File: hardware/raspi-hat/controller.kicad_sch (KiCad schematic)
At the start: 5 parts, among them J1 Conn_02x05_Counter_Clockwise, U1 STSPIN32G4, Y1 Crystal_GND23_Small

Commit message: added op amp parts to pcb
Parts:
- added C8: 100n, Capacitor_SMD:C_0603_1608Metric, symbol Device:C
- added R20, R4: 0, Resistor_SMD:R_0603_1608Metric, symbol Device:R
- added R21: 68k, Resistor_SMD:R_0603_1608Metric, symbol Device:R
- added R22: 3k3, Resistor_SMD:R_0603_1608Metric, symbol Device:R
- U1: footprint QFN_IN32G4_STM -> Package_DFN_QFN:QFN-64-1EP_8x8mm_P0.4mm_EP6.5x6.5mm
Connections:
- net +3V3: now also U1.2 (VBAT), R20.1, R20.2, R4.1
- net GND: now also C8.2, R22.2
- net i2c_scl: now also U1.59 (PB8); no longer U1.48 (PA12)
- net pwr_on: now also U1.53 (PD2); no longer U1.5 (PC15)
- net at U1.13 (PA0): now also C8.1, R21.2, R22.1
- net shunt-amp/OP+: now reaches U1.14 (PA1)
- net shunt-amp/OPOUT: now reaches U1.15 (PA2)
- net shunt-amp/OP-: now reaches U1.16 (PA3)
- net shunt-amp1/OPOUT: now reaches U1.19 (PA6)
- net shunt-amp1/OP+: now reaches U1.20 (PA7)
- net shunt-amp1/OP-: now reaches U1.22 (PC5)
- net shunt-amp2/OP+: now reaches U1.23 (PB0)
- net shunt-amp2/OPOUT: now reaches U1.24 (PB1)
- net shunt-amp2/OP-: now reaches U1.25 (PB2)
- net inverter/LS1: now reaches U1.29 (GLS1)
- net inverter/LS2: now reaches U1.30 (GLS2)
- net inverter/LS3: now reaches U1.31 (GLS3)
- net inverter/OUT3: now reaches U1.36 (OUT3)
- net inverter/HS3: now reaches U1.37 (GHS3)
- net inverter/OUT2: now reaches U1.39 (OUT2)
- net inverter/HS2: now reaches U1.40 (GHS2)
- net inverter/OUT1: now reaches U1.42 (OUT1)
- net inverter/HS1: now reaches U1.43 (GHS1)
- net +12V: now reaches U1.61 (VM)
- net +12V: now also U1.64 (REGIN), R21.1
- net stspin_3V/SW: now reaches U1.62 (SW)
- net boot_1 renamed inverter/BOOT1
- net boot_2 renamed inverter/BOOT2
- net boot_3 renamed inverter/BOOT3
- new net stspin_3V/+3V3: R4.2
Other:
- added sheet inverter (inverter.kicad_sch)
- added sheet shunt-amp (shunt-amp.kicad_sch)
- added sheet shunt-amp1 (shunt-amp.kicad_sch)
- added sheet shunt-amp2 (shunt-amp.kicad_sch)
- added sheet stspin_3V (stspin_3V.kicad_sch)
- moved on the sheet: C1, C2, J1, Y1

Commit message: updatd ioc
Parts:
- added RV1: 10k, Potentiometer_SMD:Potentiometer_Bourns_3224W_Vertical, symbol Device:R_Potentiometer_Trim
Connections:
- net +3V3: now also RV1.1
- net GND: now also J1.9 (Pin_9), RV1.3
- net reset: now also J1.10 (Pin_10)
- net uart_tx: now reaches U1.45 (PA9)
- net uart_rx: now reaches U1.46 (PA10)
- net swd_io: now reaches U1.49 (PA13)
- net swd_io: now also J1.5 (Pin_5)
- net swd_clk: now reaches U1.50 (PA14)
- net swd_clk: now also J1.7 (Pin_7)
- net at U1.52 (SCREF): now also RV1.2
- net v_mc: now reaches J1.2 (Pin_2)
- net v_mc: now also J1.4 (Pin_4)
- net i2c_scl renamed boot
- net i2c_sda: no longer names the net of U1.60 (PB9)
- net inverter/OUT1 renamed phase_u
- net inverter/OUT2 renamed phase_v
- net inverter/OUT3 renamed phase_w
- net pwr_on: no longer names the net of U1.53 (PD2)

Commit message: added more parts
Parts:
- removed R20, R4: 0, Resistor_SMD:R_0603_1608Metric, symbol Device:R
- added J5: USB3_A, Connector_USB:USB3_A_Molex_48393-001, symbol Connector:USB3_A
- added JP2, JP3: Jumper_2_Open, Jumper:SolderJumper-2_P1.3mm_Open_TrianglePad1.0x1.5mm, symbol Jumper:Jumper_2_Open
- Y1: footprint Crystal:Crystal_SMD_0603-4Pin_6.0x3.5mm -> Crystal:Crystal_SMD_1210-4Pin_1.2x1.0mm_RotB
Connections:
- net +3V3: now also JP3.2 (B); no longer RV1.1, U1.1 (REG3V3), U1.2 (VBAT), U1.26 (VREF+), U1.27 (VDDA)
- net GND: now also J5.10 (SHIELD), J5.3 (D+), J5.4 (GND), J5.6 (SSRX+), J5.7 (DRAIN), J5.9 (SSTX+)
- net stspin_3V/+3V3: now also JP2.1 (A)
- net hall_1: now reaches U1.3 (PC13)
- net hall_1: now also J5.2 (D-)
- net hall_2: now reaches U1.4 (PC14)
- net hall_2: now also J5.5 (SSRX-)
- net hall_3: now reaches U1.5 (PC15)
- net hall_3: now also J5.8 (SSTX-)
- net power_on: now reaches U1.53 (PD2)
- new net +5V: J5.1 (VBUS)
- new net shunt-amp/+3V3: JP2.2 (B), JP3.1 (A), RV1.1, U1.1 (REG3V3), U1.2 (VBAT), U1.26 (VREF+), U1.27 (VDDA)
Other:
- moved on the sheet: C8, R21, R22

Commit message: added some layers
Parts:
- Y1: footprint Crystal:Crystal_SMD_1210-4Pin_1.2x1.0mm_RotB -> Crystal:Crystal_SMD_3225-4Pin_3.2x2.5mm
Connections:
- net at U1.6 (PF0): now also Y1.3; no longer Y1.4
- net at C1.1: now also Y1.4; no longer Y1.3
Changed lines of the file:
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@@
 			)
 		)
-		(property "Footprint" "Crystal:Crystal_SMD_1210-4Pin_1.2x1.0mm_RotB"
+		(property "Footprint" "Crystal:Crystal_SMD_3225-4Pin_3.2x2.5mm"
 			(at 185.42 189.23 0)
 			(effects

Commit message: routing
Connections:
- net shunt-amp/+3V3 is gone; now on net v_mc: JP2.2 (B), JP3.1 (A), RV1.1, U1.1 (REG3V3), U1.2 (VBAT), U1.26 (VREF+), U1.27 (VDDA)
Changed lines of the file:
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@@
+	)
+	(label "v_mc"
+		(at 396.24 26.67 0)
+		(effects
+			(font
+				(size 1.27 1.27)
+			)
+			(justify left bottom)
+		)
 	)
 	(label "v_mc"

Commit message: - some readability improvements - some routing updates
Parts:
- RV1: value 10k -> 50k
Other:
- moved on the sheet: JP3, RV1
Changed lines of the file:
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@@
 	)
 	(junction
+		(at 50.8 24.13)
+		(diameter 0)
+		(color 0 0 0 0)
+	)
+	(junction
 		(at 223.52 199.39)
 		(diameter 0)
@@
 	)
 	(junction
-		(at 35.56 24.13)
-		(diameter 0)
-		(color 0 0 0 0)
-	)
-	(junction
 		(at 254 26.67)
 		(diameter 0)
@@
 	(wire
 		(pts
-			(xy 336.55 134.62) (xy 349.25 134.62)
+			(xy 389.89 134.62) (xy 377.19 134.62)
 		)
 		(stroke
@@
 	(wire
 		(pts
-			(xy 49.53 26.67) (xy 95.25 26.67)
+			(xy 81.28 26.67) (xy 95.25 26.67)
+		)
+		(stroke
+			(width 0)
+			(type default)
+		)
+	)
+	(wire
+		(pts
+			(xy 50.8 24.13) (xy 396.24 24.13)
 		)
 		(stroke
@@
 	(wire
 		(pts
-			(xy 30.48 24.13) (xy 35.56 24.13)
+			(xy 30.48 24.13) (xy 50.8 24.13)
 		)
 		(stroke
@@
 	(wire
 		(pts
-			(xy 46.99 207.01) (xy 46.99 190.5)
-		)
-		(stroke
-			(width 0)
-			(type default)
-		)
-	)
-	(wire
-		(pts
 			(xy 77.47 76.2) (xy 86.36 76.2)
 		)
@@
 	(wire
 		(pts
-			(xy 336.55 143.51) (xy 349.25 143.51)
+			(xy 389.89 143.51) (xy 377.19 143.51)
 		)
 		(stroke
@@
 	(wire
 		(pts
-			(xy 250.19 176.53) (xy 248.92 176.53)
+			(xy 250.19 173.99) (xy 248.92 173.99)
 		)
 		(stroke
@@
 	(wire
 		(pts
-			(xy 254 180.34) (xy 254 241.3)
+			(xy 254 177.8) (xy 254 241.3)
 		)
 		(stroke
@@
 	(wire
 		(pts
-			(xy 254 172.72) (xy 254 26.67)
+			(xy 254 170.18) (xy 254 26.67)
 		)
 		(stroke
@@
 	(wire
 		(pts
-			(xy 336.55 135.89) (xy 349.25 135.89)
+			(xy 389.89 135.89) (xy 377.19 135.89)
 		)
 		(stroke
@@
 	(wire
 		(pts
-			(xy 35.56 24.13) (xy 396.24 24.13)
-		)
-		(stroke
-			(width 0)
-			(type default)
-		)
-	)
-	(wire
-		(pts
 			(xy 231.14 21.59) (xy 231.14 58.42)
 		)
@@
 	(wire
 		(pts
-			(xy 248.92 176.53) (xy 248.92 181.61)
+			(xy 248.92 173.99) (xy 248.92 181.61)
 		)
 		(stroke
@@
 	(wire
 		(pts
+			(xy 50.8 207.01) (xy 46.99 207.01)
+		)
+		(stroke
+			(width 0)
+			(type default)
+		)
+	)
+	(wire
+		(pts
 			(xy 363.22 147.32) (xy 363.22 241.3)
 		)
@@
 	(wire
 		(pts
-			(xy 336.55 142.24) (xy 349.25 142.24)
+			(xy 389.89 142.24) (xy 377.19 142.24)
 		)
 		(stroke
@@
 	(wire
 		(pts
-			(xy 336.55 138.43) (xy 349.25 138.43)
+			(xy 389.89 138.43) (xy 377.19 138.43)
 		)
 		(stroke
@@
 	(wire
 		(pts
-			(xy 46.99 190.5) (xy 35.56 190.5)
-		)
-		(stroke
-			(width 0)
-			(type default)
-		)
-	)
-	(wire
-		(pts
 			(xy 31.75 234.95) (xy 31.75 241.3)
 		)
@@
 	(wire
 		(pts
-			(xy 336.55 139.7) (xy 349.25 139.7)
+			(xy 389.89 139.7) (xy 377.19 139.7)
 		)
 		(stroke
@@
 	(wire
 		(pts
-			(xy 35.56 190.5) (xy 35.56 24.13)
+			(xy 50.8 24.13) (xy 50.8 207.01)
 		)
 		(stroke
@@
 	(wire
 		(pts
-			(xy 30.48 26.67) (xy 39.37 26.67)
+			(xy 30.48 26.67) (xy 71.12 26.67)
 		)
 		(stroke
@@
 	)
 	(label "shunt3_h"
-		(at 336.55 142.24 180)
+		(at 389.89 142.24 0)
 		(effects
 			(font
 				(size 1.27 1.27)
 			)
-			(justify right bottom)
+			(justify left bottom)
 		)
 	)
@@
 	)
 	(label "shunt2_l"
-		(at 336.55 139.7 180)
+		(at 389.89 139.7 0)
 		(effects
 			(font
 				(size 1.27 1.27)
 			)
-			(justify right bottom)
+			(justify left bottom)
 		)
 	)
@@
 	)
 	(label "shunt1_l"
-		(at 336.55 135.89 180)
+		(at 389.89 135.89 0)
 		(effects
 			(font
 				(size 1.27 1.27)
 			)
-			(justify right bottom)
+			(justify left bottom)
 		)
 	)
@@
 	)
 	(label "shunt3_l"
-		(at 336.55 143.51 180)
+		(at 389.89 143.51 0)
 		(effects
 			(font
 				(size 1.27 1.27)
 			)
-			(justify right bottom)
+			(justify left bottom)
 		)
 	)
 	(label "shunt2_h"
-		(at 336.55 138.43 180)
+		(at 389.89 138.43 0)
 		(effects
 			(font
 				(size 1.27 1.27)
 			)
-			(justify right bottom)
+			(justify left bottom)
 		)
 	)
@@
 	)
 	(label "shunt1_h"
-		(at 336.55 134.62 180)
+		(at 389.89 134.62 0)
 		(effects
 			(font
 				(size 1.27 1.27)
 			)
-			(justify right bottom)
+			(justify left bottom)
 		)
 	)
@@
 	(symbol
 		(lib_id "Jumper:Jumper_2_Open")
-		(at 44.45 26.67 180)
+		(at 76.2 26.67 180)
 		(unit 1)
 		(exclude_from_sim no)
@@
 		(dnp no)
 		(property "Reference" "JP3"
-			(at 38.1 28.194 0)
+			(at 69.85 28.194 0)
 			(effects
 				(font
@@
 		)
 		(property "Value" "Jumper_2_Open"
-			(at 37.846 30.48 0)
+			(at 69.596 30.48 0)
 			(effects
 				(font
@@
 		)
 		(property "Footprint" "Jumper:SolderJumper-2_P1.3mm_Open_TrianglePad1.0x1.5mm"
-			(at 44.45 26.67 0)
+			(at 76.2 26.67 0)
 			(effects
 				(font
@@
 		)
 		(property "Datasheet" "~"
-			(at 44.45 26.67 0)
+			(at 76.2 26.67 0)
 			(effects
 				(font
@@
 		)
 		(property "Description" "Jumper, 2-pole, open"
-			(at 44.45 26.67 0)
+			(at 76.2 26.67 0)
 			(effects
 				(font
@@
 	(symbol
 		(lib_id "Device:R_Potentiometer_Trim")
-		(at 254 176.53 0)
+		(at 254 173.99 0)
 		(mirror y)
 		(unit 1)
@@
 		(dnp no)
 		(property "Reference" "RV1"
-			(at 256.54 175.2599 0)
+			(at 256.54 172.7199 0)
 			(effects
 				(font
@@
 			)
 		)
-		(property "Value" "10k"
-			(at 254 174.498 90)
+		(property "Value" "50k"
+			(at 254 171.958 90)
 			(effects
 				(font
@@
 		)
 		(property "Footprint" "Potentiometer_SMD:Potentiometer_Bourns_3224W_Vertical"
-			(at 254 176.53 0)
+			(at 254 173.99 0)
 			(effects
 				(font
@@
 		)
 		(property "Datasheet" "~"
-			(at 254 176.53 0)
+			(at 254 173.99 0)
 			(effects
 				(font
@@
 		)
 		(property "Description" "Trim-potentiometer"
-			(at 254 176.53 0)
+			(at 254 173.99 0)
 			(effects
 				(font
@@
 		)
 		(pin "SHUNT1_H" input
-			(at 349.25 134.62 180)
+			(at 377.19 134.62 0)
 			(effects
 				(font
 					(size 1.27 1.27)
 				)
-				(justify left)
+				(justify right)
 			)
 		)
 		(pin "SHUNT1_L" input
-			(at 349.25 135.89 180)
+			(at 377.19 135.89 0)
 			(effects
 				(font
 					(size 1.27 1.27)
 				)
-				(justify left)
+				(justify right)
 			)
 		)
 		(pin "SHUNT2_H" input
-			(at 349.25 138.43 180)
+			(at 377.19 138.43 0)
 			(effects
 				(font
 					(size 1.27 1.27)
 				)
-				(justify left)
+				(justify right)
 			)
 		)
 		(pin "SHUNT2_L" input
-			(at 349.25 139.7 180)
+			(at 377.19 139.7 0)
 			(effects
 				(font
 					(size 1.27 1.27)
 				)
-				(justify left)
+				(justify right)
 			)
 		)
 		(pin "SHUNT3_H" input
-			(at 349.25 142.24 180)
+			(at 377.19 142.24 0)
 			(effects
 				(font
 					(size 1.27 1.27)
 				)
-				(justify left)
+				(justify right)
 			)
 		)
 		(pin "SHUNT3_L" input
-			(at 349.25 143.51 180)
+			(at 377.19 143.51 0)
 			(effects
 				(font
 					(size 1.27 1.27)
 				)
-				(justify left)
+				(justify right)
 			)
 		)

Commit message: adapted some parts
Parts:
- J5: footprint Connector_USB:USB3_A_Molex_48393-001 -> Connector_USB:USB3_A_Receptacle_Wuerth_692122030100
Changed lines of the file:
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@@
 			)
 		)
-		(property "Footprint" "Connector_USB:USB3_A_Molex_48393-001"
+		(property "Footprint" "Connector_USB:USB3_A_Receptacle_Wuerth_692122030100"
 			(at 38.1 214.63 0)
 			(effects

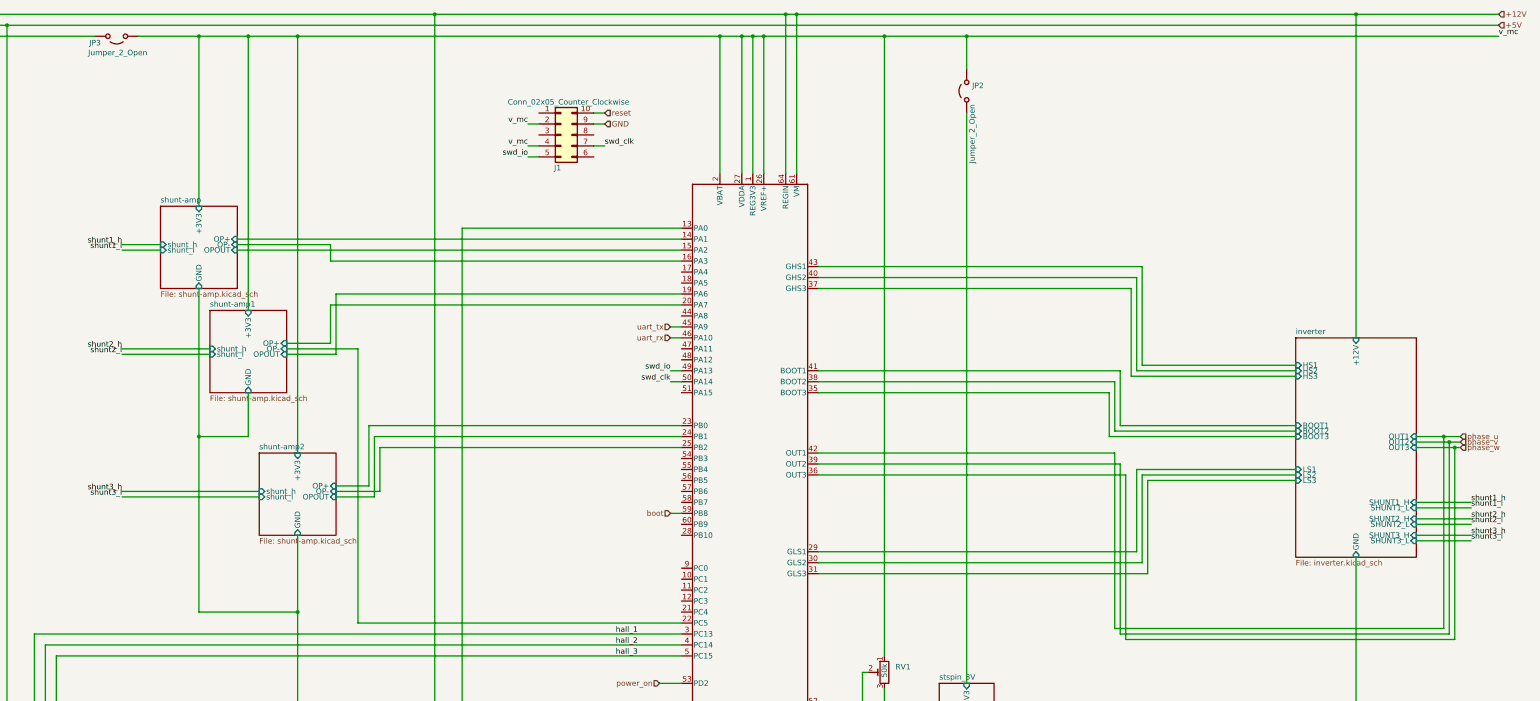
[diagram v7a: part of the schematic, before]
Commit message: - added ntc for temperature sensing - documented calculation for ntc voltage output in software/docs/ntc.ipynb - added gnd planes for all layers
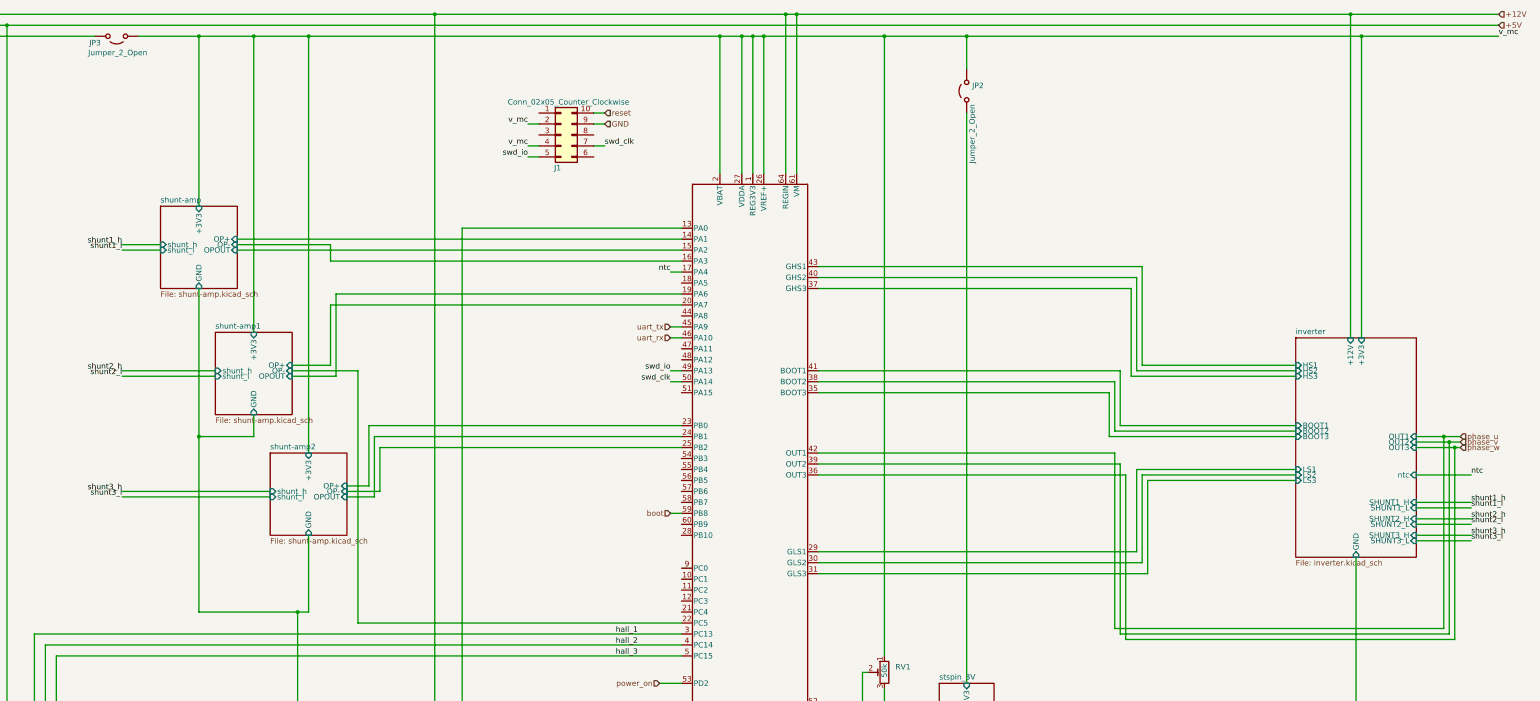
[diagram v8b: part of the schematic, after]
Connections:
- net ntc: now reaches U1.17 (PA4)
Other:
- sheet inverter ports: added +3V3, ntc; removed none
